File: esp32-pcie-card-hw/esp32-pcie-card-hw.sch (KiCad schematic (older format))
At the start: 46 parts, among them J4 KH-IPEX-K501-29, SW1 PTS636 SM43 SMTR LFS, SW2 PTS636 SM43 SMTR LFS, U3 ATECC608A-MAHDA, U4 TLV75733, U5 W25Q64JVSSIQ, U6 ESP32, Y2 40MHz 10ppm 3225

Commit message: WIP on schematics
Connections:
- net ESP_BOOT: now also R37.2, SW1.1 (A)
- removed net BTN_USER: R37.2, SW1.1 (A), U6.5 (SENSOR_VP(GPI36/ADC1:0/RTC0))
- net ETH_CLK: no longer names the net of U6.27 ((HS1_DATA5)GPIO17)
- net ETH_CRS: no longer names the net of U6.16 ((ADC2:7/TOUCH7/RTC17)GPIO27)
- net ETH_MDC: no longer names the net of U6.25 ((HS1_DATA4)GPIO16)
- net ETH_MDIO: no longer names the net of U6.35 ((VSPICLK/HS1_DATA7)GPIO18)
- net ETH_RXD+: no longer names the net of U6.15 ((DAC2/ADC2:9/RTC7)GPIO26)
- net ETH_RXD-: no longer names the net of U6.14 ((DAC1/ADC2:8/RTC6)GPIO25)
- net ETH_TXD+: no longer names the net of U6.39 ((VSPIWP/HS2_CLK)GPIO22)
- net ETH_TXD-: no longer names the net of U6.38 ((VSPIQ/HS2_DATA2)GPIO19)
- net ETH_TXEN: no longer names the net of U6.42 ((VSPIHD/HS2_CMD)GPIO21)
- net EXP_RX: no longer names the net of U6.10 (VDET_1(GPI34/ADC1:6))
- net EXP_TX: no longer names the net of U6.20 ((GPIO13/ADC2:4/TOUCH4/RTC14/SPID/U0CTS)MTCK)
- net P_BUZZER: no longer names the net of U6.24 ((ADC2:0/TOUCH0/RTC10/SPIHD)GPIO4)
- net RGB_B: no longer names the net of U6.13 (32K_XN(GPIO33/ADC1:5/TOUCH8/RTC8))
- net RGB_G: no longer names the net of U6.12 (32K_XP(GPIO32/ADC1:4/TOUCH9/RTC9))
- net RGB_R: no longer names the net of U6.17 ((GPIO14/ADC2:6/TOUCH6/RTC16/SPICLK)MTMS)
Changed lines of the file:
@@
 	4600 2150 4750 2150
 Wire Wire Line
-	10200 3800 10300 3800
-Wire Wire Line
 	10200 1300 10300 1300
 Wire Wire Line
 	10200 1400 10300 1400
 Wire Wire Line
-	10200 1500 10300 1500
-Wire Wire Line
-	10200 1600 10300 1600
-Wire Wire Line
-	10200 1700 10300 1700
-Wire Wire Line
-	10200 1800 10300 1800
-Wire Wire Line
-	10200 1900 10300 1900
-Wire Wire Line
-	10200 2000 10300 2000
-Wire Wire Line
-	10200 2200 10300 2200
-Wire Wire Line
-	10200 2300 10300 2300
-Wire Wire Line
-	10200 2400 10300 2400
-Wire Wire Line
-	10200 2500 10300 2500
-Wire Wire Line
-	10200 2600 10300 2600
-Wire Wire Line
-	10200 2700 10300 2700
-Wire Wire Line
 	10200 3000 10300 3000
 Wire Wire Line
@@
 Wire Wire Line
 	10200 3500 10300 3500
-Wire Wire Line
-	6200 3200 6100 3200
 $Comp
 L Device:R_US R30
@@
 Text GLabel 10300 3500 2    50   Output ~ 0
 FLASH_CS
-Text GLabel 10300 1500 2    50   Output ~ 0
-P_BUZZER
 $Comp
 L power:+3V3 #PWR0127
@@
 Wire Notes Line
 	4500 1600 4500 2700
-Wire Wire Line
-	6200 2800 6100 2800
-Wire Wire Line
-	6200 2400 6100 2400
-Wire Wire Line
-	6200 2500 6100 2500
-Text GLabel 10300 1600 2    50   BiDi ~ 0
-CRYPTO_SCL
-Text GLabel 10300 1700 2    50   BiDi ~ 0
-ETH_MDC
-Text GLabel 10300 1800 2    50   BiDi ~ 0
-ETH_CLK
-Text GLabel 10300 1900 2    50   BiDi ~ 0
-ETH_MDIO
-Text GLabel 10300 2000 2    50   BiDi ~ 0
-ETH_TXD-
-Text GLabel 10300 2200 2    50   BiDi ~ 0
-ETH_TXEN
-Text GLabel 10300 2300 2    50   BiDi ~ 0
-ETH_TXD+
-Text GLabel 10300 2400 2    50   BiDi ~ 0
-CRYPTO_SDA
-Text GLabel 10300 2500 2    50   BiDi ~ 0
-ETH_RXD-
-Text GLabel 10300 2600 2    50   BiDi ~ 0
-ETH_RXD+
-Text GLabel 10300 2700 2    50   BiDi ~ 0
-ETH_CRS
-Text GLabel 10300 3800 2    50   Output ~ 0
-EXP_TX
-Text GLabel 6100 3200 0    50   Input ~ 0
-BTN_USER
-Text GLabel 6100 2800 0    50   Input ~ 0
-EXP_RX
 $Comp
 L Device:C_Small C32
@@
 Wire Notes Line
 	950  1750 4300 1750
-Text GLabel 6100 2500 0    50   Output ~ 0
-RGB_B
-Text GLabel 6100 2400 0    50   Output ~ 0
-RGB_G
 Text GLabel 10300 1400 2    50   Output ~ 0
 GPIO2
@@
 Text GLabel 10300 3700 2    50   Output ~ 0
 GPIO12
-Wire Wire Line
-	10200 3900 10300 3900
-Text GLabel 10300 3900 2    50   Output ~ 0
-RGB_R
 Text GLabel 1850 1350 0    50   Input ~ 0
 CRYPTO_SCL
@@
 $EndComp
 Text GLabel 8500 5150 0    50   Input ~ 0
-BTN_USER
+ESP_BOOT
 $Comp
 L Device:R_US R37
@@
 F1 "usb-serial.sch" 50
 $EndSheet
+Wire Wire Line
+	10200 2400 10300 2400
+Text GLabel 10300 2400 2    50   BiDi ~ 0
+CRYPTO_SDA
+Wire Wire Line
+	10200 1600 10300 1600
+Text GLabel 10300 1600 2    50   BiDi ~ 0
+CRYPTO_SCL
 $EndSCHEMATC

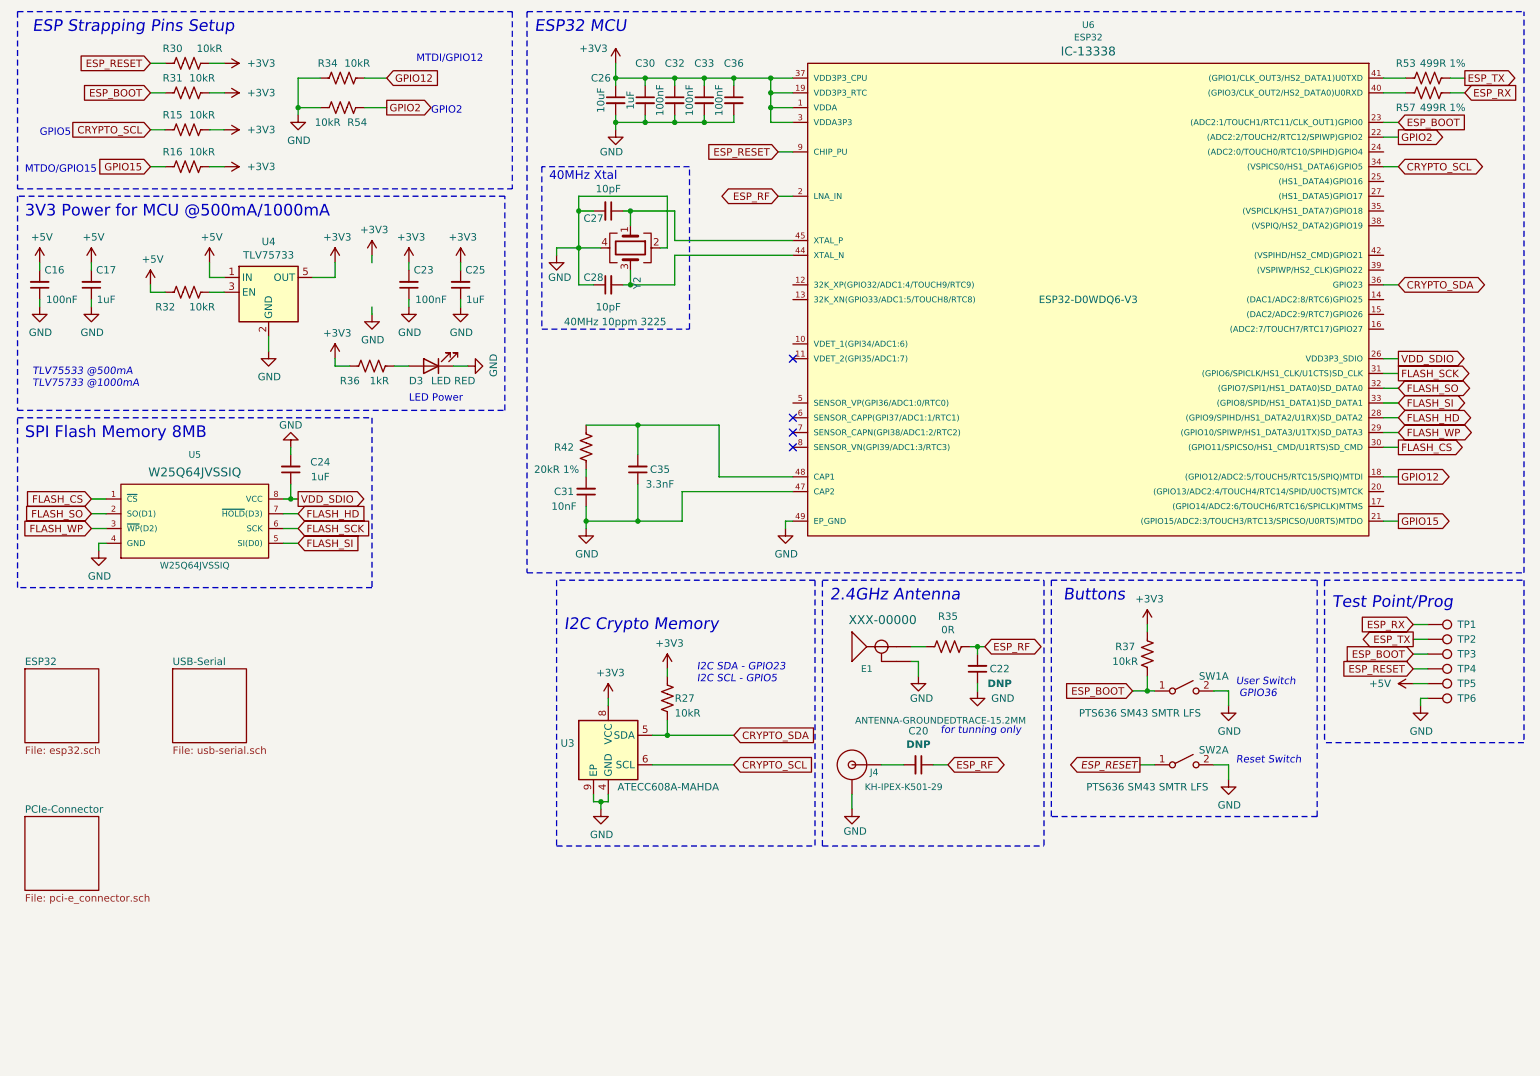
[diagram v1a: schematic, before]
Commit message: Added JTAG 10pin connector
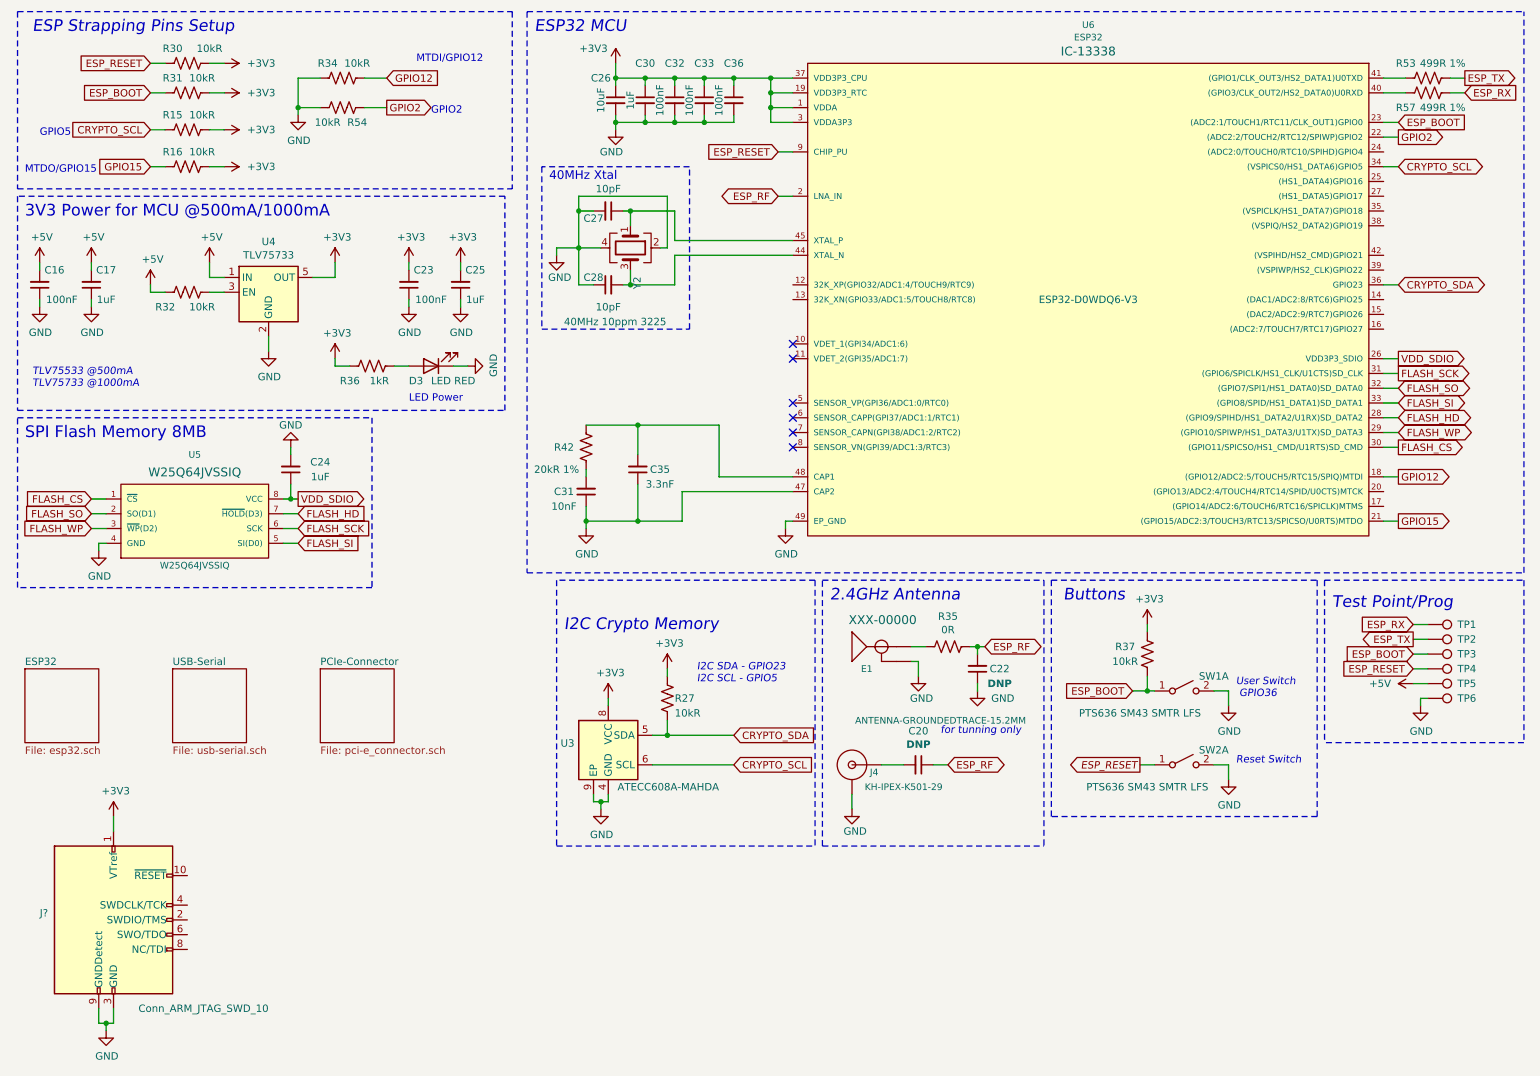
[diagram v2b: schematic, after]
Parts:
- added J?: Conn_ARM_JTAG_SWD_10, symbol Connector:Conn_ARM_JTAG_SWD_10
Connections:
- net +3V3: now also J?.1 (VTref)
- net GND: now also J?.3 (GND), J?.5 (GND), J?.9 (GNDDetect)
- no-connect marks 4 -> 6
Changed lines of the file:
@@
 Text Notes 1050 3100 0    50   Italic 0
 TLV75533 @500mA\nTLV75733 @1000mA\n
-Wire Wire Line
-	3350 2550 3350 2600
-Wire Wire Line
-	3350 2250 3350 2200
-$Comp
-L power:GND #PWR0183
-U 1 1 5F2E4945
-P 3350 2600
-F 0 "#PWR0183" H 3350 2350 50  0001 C CNN
-F 1 "GND" H 3355 2427 50  0000 C CNN
-F 2 "" H 3350 2600 50  0001 C CNN
-F 3 "" H 3350 2600 50  0001 C CNN
-	1    3350 2600
-	1    0    0    -1
-$EndComp
 $Comp
 L Device:Crystal_GND24 Y2
@@
 FLASH_SI
 $Comp
-L power:+3V3 #PWR0197
-U 1 1 5F33E954
-P 3350 2200
-F 0 "#PWR0197" H 3350 2050 50  0001 C CNN
-F 1 "+3V3" H 3365 2373 50  0000 C CNN
-F 2 "" H 3350 2200 50  0001 C CNN
-F 3 "" H 3350 2200 50  0001 C CNN
-	1    3350 2200
-	1    0    0    -1
-$EndComp
-$Comp
 L power:+3V3 #PWR0198
 U 1 1 5F33ED37
@@
 $EndComp
 $Sheet
-S 1000 6000 500  500
+S 3000 5000 500  500
 U 60B56722
 F0 "PCIe-Connector" 50
@@
 Text GLabel 10300 1600 2    50   BiDi ~ 0
 CRYPTO_SCL
+NoConn ~ 6200 2800
+NoConn ~ 6200 3200
+$Comp
+L Connector:Conn_ARM_JTAG_SWD_10 J?
+U 1 1 604AE2F1
+P 1600 6700
+F 0 "J?" H 1157 6746 50  0000 R CNN
+F 1 "Conn_ARM_JTAG_SWD_10" H 2650 6100 50  0000 R CNN
+F 2 "" H 1600 6700 50  0001 C CNN
+F 3 "http://infocenter.arm.com/help/topic/com.arm.doc.ddi0314h/DDI0314H_coresight_components_trm.pdf" V 1250 5450 50  0001 C CNN
+	1    1600 6700
+	1    0    0    -1
+$EndComp
+$Comp
+L power:GND #PWR?
+U 1 1 604B0F40
+P 1550 7450
+F 0 "#PWR?" H 1550 7200 50  0001 C CNN
+F 1 "GND" H 1555 7277 50  0000 C CNN
+F 2 "" H 1550 7450 50  0001 C CNN
+F 3 "" H 1550 7450 50  0001 C CNN
+	1    1550 7450
+	1    0    0    -1
+$EndComp
+Wire Wire Line
+	1500 7300 1500 7400
+Wire Wire Line
+	1500 7400 1550 7400
+Wire Wire Line
+	1600 7400 1600 7300
+Wire Wire Line
+	1550 7450 1550 7400
+Connection ~ 1550 7400
+Wire Wire Line
+	1550 7400 1600 7400
+$Comp
+L power:+3V3 #PWR?
+U 1 1 604C3267
+P 1600 6000
+F 0 "#PWR?" H 1600 5850 50  0001 C CNN
+F 1 "+3V3" H 1615 6173 50  0000 C CNN
+F 2 "" H 1600 6000 50  0001 C CNN
+F 3 "" H 1600 6000 50  0001 C CNN
+	1    1600 6000
+	1    0    0    -1
+$EndComp
+Wire Wire Line
+	1600 6000 1600 6100
 $EndSCHEMATC

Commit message: WIP
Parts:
- J1: renamed from J?; footprint (none) -> Connector_PinSocket_1.27mm:PinSocket_2x05_P1.27mm_Vertical_SMD
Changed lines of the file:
@@
 NoConn ~ 6200 3200
 $Comp
-L Connector:Conn_ARM_JTAG_SWD_10 J?
+L Connector:Conn_ARM_JTAG_SWD_10 J1
 U 1 1 604AE2F1
 P 1600 6700
-F 0 "J?" H 1157 6746 50  0000 R CNN
+F 0 "J1" H 1157 6746 50  0000 R CNN
 F 1 "Conn_ARM_JTAG_SWD_10" H 2650 6100 50  0000 R CNN
-F 2 "" H 1600 6700 50  0001 C CNN
+F 2 "Connector_PinSocket_1.27mm:PinSocket_2x05_P1.27mm_Vertical_SMD" H 1600 6700 50  0001 C CNN
 F 3 "http://infocenter.arm.com/help/topic/com.arm.doc.ddi0314h/DDI0314H_coresight_components_trm.pdf" V 1250 5450 50  0001 C CNN
 	1    1600 6700
@@
 $EndComp
 $Comp
-L power:GND #PWR?
+L power:GND #PWR0107
 U 1 1 604B0F40
 P 1550 7450
-F 0 "#PWR?" H 1550 7200 50  0001 C CNN
+F 0 "#PWR0107" H 1550 7200 50  0001 C CNN
 F 1 "GND" H 1555 7277 50  0000 C CNN
 F 2 "" H 1550 7450 50  0001 C CNN
@@
 	1550 7400 1600 7400
 $Comp
-L power:+3V3 #PWR?
+L power:+3V3 #PWR0108
 U 1 1 604C3267
 P 1600 6000
-F 0 "#PWR?" H 1600 5850 50  0001 C CNN
+F 0 "#PWR0108" H 1600 5850 50  0001 C CNN
 F 1 "+3V3" H 1615 6173 50  0000 C CNN
 F 2 "" H 1600 6000 50  0001 C CNN
